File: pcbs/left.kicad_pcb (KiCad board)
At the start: 2 copper layers, 121.1 x 91.2 mm, 27 parts

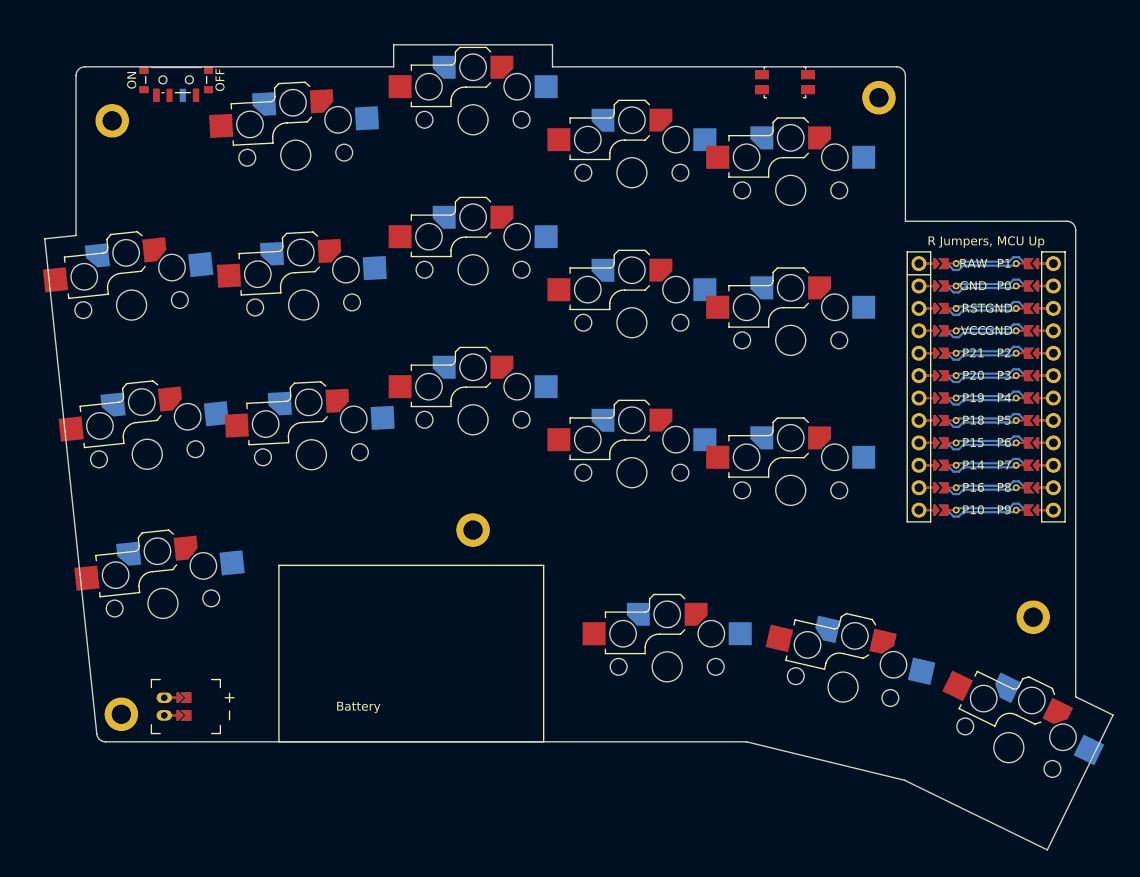
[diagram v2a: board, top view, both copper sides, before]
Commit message: Add tons of expands
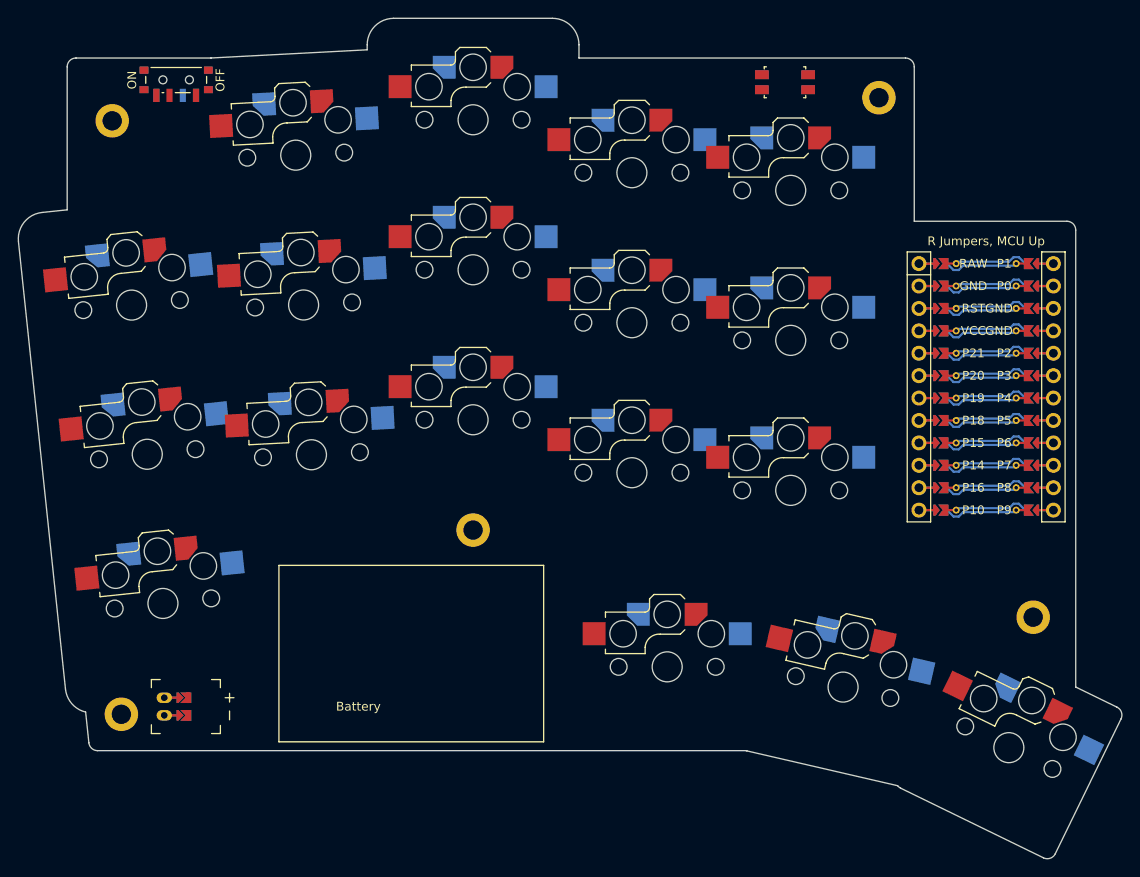
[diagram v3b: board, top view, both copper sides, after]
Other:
- board size 121.1 x 91.2 mm -> 125.1 x 95.2 mm
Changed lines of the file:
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@@
     (fp_circle (center 0 0) (end -2.1500000000000004 0) (layer "B.CrtYd") (stroke (width 0.05) (type solid)) (fill none))
   )
-  (gr_line (start 86.60684319999999 58.67357570000001) (end 92.50479308505149 114.78881969999998) (layer Edge.Cuts) (stroke (width 0.15) (type default)))
-(gr_line (start 86.60684319999999 58.67357570000001) (end 90.1483667 58.30134658019551) (layer Edge.Cuts) (stroke (width 0.15) (type default)))
-(gr_line (start 144.1483666 39.18429119999999) (end 144.1483667 36.68429119999999) (layer Edge.Cuts) (stroke (width 0.15) (type default)))
-(gr_line (start 144.1483667 36.68429119999999) (end 126.1483667 36.68429119999999) (layer Edge.Cuts) (stroke (width 0.15) (type default)))
-(gr_line (start 126.1483667 36.68429119999999) (end 126.1483667 39.18429119999999) (layer Edge.Cuts) (stroke (width 0.15) (type default)))
-(gr_line (start 93.49931498505148 115.68429119999999) (end 166.1483666 115.68429119999999) (layer Edge.Cuts) (stroke (width 0.15) (type default)))
-(gr_line (start 184.0527886 120.0396531) (end 200.23108150000002 127.93033369999999) (layer Edge.Cuts) (stroke (width 0.15) (type default)))
-(gr_line (start 200.23108150000002 127.93033369999999) (end 207.683391 112.65083489999999) (layer Edge.Cuts) (stroke (width 0.15) (type default)))
-(gr_line (start 207.683391 112.65083489999999) (end 203.4483666 110.58527550630113) (layer Edge.Cuts) (stroke (width 0.15) (type default)))
-(gr_line (start 184.0527886 120.0396531) (end 166.1483666 115.68429119999999) (layer Edge.Cuts) (stroke (width 0.15) (type default)))
-(gr_line (start 184.1483667 56.684291099999996) (end 202.4483666 56.684291099999996) (layer Edge.Cuts) (stroke (width 0.15) (type default)))
+  (gr_line (start 147.1483666 38.18429119999999) (end 147.1483667 36.68429119999999) (layer Edge.Cuts) (stroke (width 0.15) (type default)))
+(gr_arc (start 147.1483667 36.68429119999999) (mid 146.269687 34.56297079999999) (end 144.1483667 33.68429119999999) (layer Edge.Cuts) (stroke (width 0.15) (type default)))
+(gr_line (start 144.1483667 33.68429119999999) (end 126.1483667 33.68429119999999) (layer Edge.Cuts) (stroke (width 0.15) (type default)))
+(gr_arc (start 126.1483667 33.68429119999999) (mid 124.0270464 34.56297089999999) (end 123.1483667 36.68429119999999) (layer Edge.Cuts) (stroke (width 0.15) (type default)))
+(gr_line (start 123.1483667 36.68429119999999) (end 123.1483667 37.25485987602707) (layer Edge.Cuts) (stroke (width 0.15) (type default)))
+(gr_line (start 123.1483667 37.25485987602707) (end 105.4622228 38.1817515) (layer Edge.Cuts) (stroke (width 0.15) (type default)))
+(gr_arc (start 105.4617762 38.1817748) (mid 105.4406227 38.1829583) (end 105.41947809999999 38.1842912) (layer Edge.Cuts) (stroke (width 0.15) (type default)))
+(gr_line (start 89.1483667 55.3899259419181) (end 86.29325769999998 55.69001000000001) (layer Edge.Cuts) (stroke (width 0.15) (type default)))
+(gr_arc (start 86.29325779999999 55.69001000000001) (mid 84.27540529999999 56.78561460000001) (end 83.62327749999999 58.98716120000001) (layer Edge.Cuts) (stroke (width 0.15) (type default)))
+(gr_line (start 83.6232775 58.98716120000001) (end 88.9542292 109.7077778) (layer Edge.Cuts) (stroke (width 0.15) (type default)))
+(gr_arc (start 88.9542292 109.7077778) (mid 89.6827724 111.3727962) (end 91.2389242 112.3116535) (layer Edge.Cuts) (stroke (width 0.15) (type default)))
+(gr_line (start 92.5989109 116.68429119999999) (end 166.0842466 116.68429119999999) (layer Edge.Cuts) (stroke (width 0.15) (type default)))
+(gr_arc (start 166.0842466 116.68429119999999) (mid 166.12960690000003 116.6982274) (end 166.17557730000001 116.70999599999999) (layer Edge.Cuts) (stroke (width 0.15) (type default)))
+(gr_line (start 166.17557730000001 116.70999599999999) (end 183.2648105 120.6553563) (layer Edge.Cuts) (stroke (width 0.15) (type default)))
+(gr_arc (start 183.2648105 120.6553563) (mid 183.4234888 120.81681569999999) (end 183.6144175 120.93844709999999) (layer Edge.Cuts) (stroke (width 0.15) (type default)))
+(gr_line (start 183.61481949999998 120.9386431) (end 199.79230840000002 128.8289316) (layer Edge.Cuts) (stroke (width 0.15) (type default)))
+(gr_arc (start 199.7927104 128.8291277) (mid 200.5566497 128.8758522) (end 201.12987550000003 128.3687048) (layer Edge.Cuts) (stroke (width 0.15) (type default)))
+(gr_line (start 201.1300715 128.36830279999998) (end 208.5819889 113.089608) (layer Edge.Cuts) (stroke (width 0.15) (type default)))
+(gr_arc (start 208.58218500000004 113.08920599999999) (mid 208.62890950000002 112.32526669999999) (end 208.12176210000004 111.7520409) (layer Edge.Cuts) (stroke (width 0.15) (type default)))
+(gr_line (start 208.12136010000003 111.7518449) (end 203.4483666 109.4726736947813) (layer Edge.Cuts) (stroke (width 0.15) (type default)))
+(gr_line (start 185.1483667 56.684291099999996) (end 202.4483666 56.684291099999996) (layer Edge.Cuts) (stroke (width 0.15) (type default)))
 (gr_arc (start 203.4483666 57.684291099999996) (mid 203.1554734 56.9771843) (end 202.4483666 56.684291099999996) (layer Edge.Cuts) (stroke (width 0.15) (type default)))
-(gr_line (start 203.4483666 57.684291099999996) (end 203.4483666 110.58527550630113) (layer Edge.Cuts) (stroke (width 0.15) (type default)))
-(gr_arc (start 92.50479308505149 114.78881969999996) (mid 92.83018438505148 115.42743599999996) (end 93.49931498505148 115.68429119999996) (layer Edge.Cuts) (stroke (width 0.15) (type default)))
-(gr_line (start 90.1483667 58.30134658019551) (end 90.1483667 40.18429119999999) (layer Edge.Cuts) (stroke (width 0.15) (type default)))
-(gr_line (start 91.1483667 39.18429119999999) (end 126.1483667 39.18429119999999) (layer Edge.Cuts) (stroke (width 0.15) (type default)))
-(gr_line (start 144.1483666 39.18429119999999) (end 183.1483667 39.18429119999999) (layer Edge.Cuts) (stroke (width 0.15) (type default)))
-(gr_line (start 184.1483667 40.18429119999999) (end 184.1483667 56.684291099999996) (layer Edge.Cuts) (stroke (width 0.15) (type default)))
-(gr_arc (start 91.1483667 39.18429119999999) (mid 90.44125989999999 39.47718439999999) (end 90.1483667 40.18429119999999) (layer Edge.Cuts) (stroke (width 0.15) (type default)))
-(gr_arc (start 184.1483667 40.18429119999999) (mid 183.8554735 39.47718439999999) (end 183.1483667 39.18429119999999) (layer Edge.Cuts) (stroke (width 0.15) (type default)))
+(gr_line (start 203.4483666 57.684291099999996) (end 203.4483666 109.4726736947813) (layer Edge.Cuts) (stroke (width 0.15) (type default)))
+(gr_line (start 91.60438903481348 115.78881969999996) (end 91.2389242 112.3116535) (layer Edge.Cuts) (stroke (width 0.15) (type default)))
+(gr_arc (start 91.60438903481348 115.78881969999996) (mid 91.92978033481347 116.42743599999996) (end 92.59891093481347 116.68429119999996) (layer Edge.Cuts) (stroke (width 0.15) (type default)))
+(gr_line (start 89.1483667 55.3899259419181) (end 89.1483667 39.18429119999999) (layer Edge.Cuts) (stroke (width 0.15) (type default)))
+(gr_arc (start 90.1483667 38.18429119999999) (mid 89.44125989999999 38.47718439999999) (end 89.1483667 39.18429119999999) (layer Edge.Cuts) (stroke (width 0.15) (type default)))
+(gr_line (start 90.1483667 38.18429119999999) (end 105.41947809999999 38.1842912) (layer Edge.Cuts) (stroke (width 0.15) (type default)))
+(gr_line (start 147.1483666 38.18429119999999) (end 184.1483667 38.18429119999999) (layer Edge.Cuts) (stroke (width 0.15) (type default)))
+(gr_arc (start 185.1483667 39.18429119999999) (mid 184.8554735 38.47718439999999) (end 184.1483667 38.18429119999999) (layer Edge.Cuts) (stroke (width 0.15) (type default)))
+(gr_line (start 185.1483667 39.18429119999999) (end 185.1483667 56.684291099999996) (layer Edge.Cuts) (stroke (width 0.15) (type default)))
 (gr_line (start 113.1483666 95.68429119999999) (end 113.1483666 115.68429119999999) (layer F.SilkS) (stroke (width 0.15) (type default)))
 (gr_line (start 113.1483666 115.68429119999999) (end 143.1483666 115.68429119999999) (layer F.SilkS) (stroke (width 0.15) (type default)))

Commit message: Add filled zone
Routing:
- added copper zone on F.Cu, net GND
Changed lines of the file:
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@@
   (title_block
     (title "left")
-    (date "2024-11-22")
+    (date "2024-11-23")
     (rev "v1.0.0")
     (company "Unknown")
@@
     (fp_circle (center 0 0) (end -2.1500000000000004 0) (layer "B.CrtYd") (stroke (width 0.05) (type solid)) (fill none))
   )
+  (zone
+    (net 2)
+    (net_name "GND")
+    (locked no)
+    (layers "F.Cu")
+    (hatch edge 0.5)
+    (connect_pads
+      (clearance 0.508)
+    )
+    (min_thickness 0.25)
+    (filled_areas_thickness no)
+    (fill
+      yes
+      (thermal_gap 0.5)
+      (thermal_bridge_width 0.5)
+      (smoothing chamfer)
+      (radius 0.5)
+      (island_removal_mode 1)
+      (island_area_min 5)
+    )
+    (polygon
+      (pts
+        (xy 0 0) (xy 420 0) (xy 420 297) (xy 0 297)
+      )
+    )
+  )
   (gr_line (start 147.1483666 38.18429119999999) (end 147.1483667 36.68429119999999) (layer Edge.Cuts) (stroke (width 0.15) (type default)))
